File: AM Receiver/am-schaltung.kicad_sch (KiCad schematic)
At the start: 43 parts, among them IC100 SA612AD, IC103 TDA1072AT, P100 10k 25% Trimmer, Q100 MMBFJ310LT3G, Q101 MMBFJ310LT3G

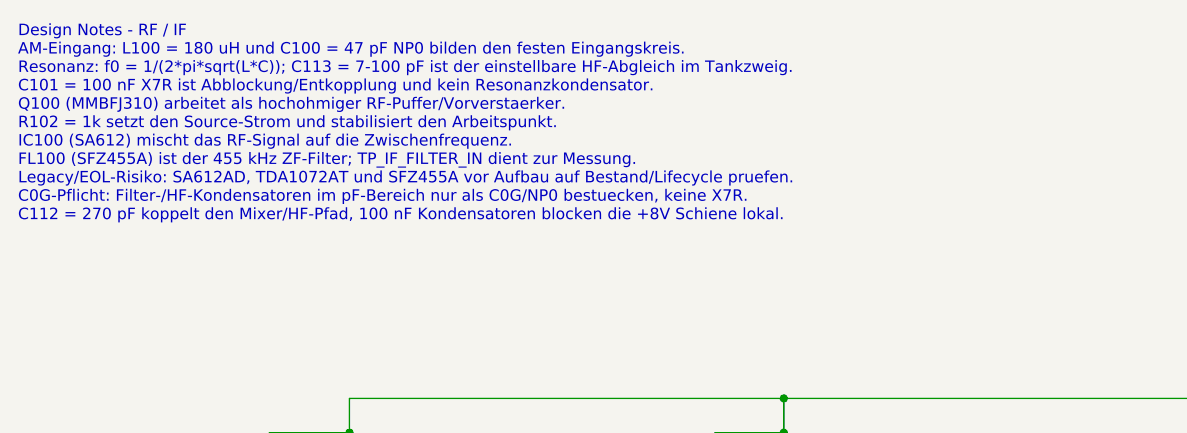
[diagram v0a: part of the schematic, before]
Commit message: updated schematic root page voltage
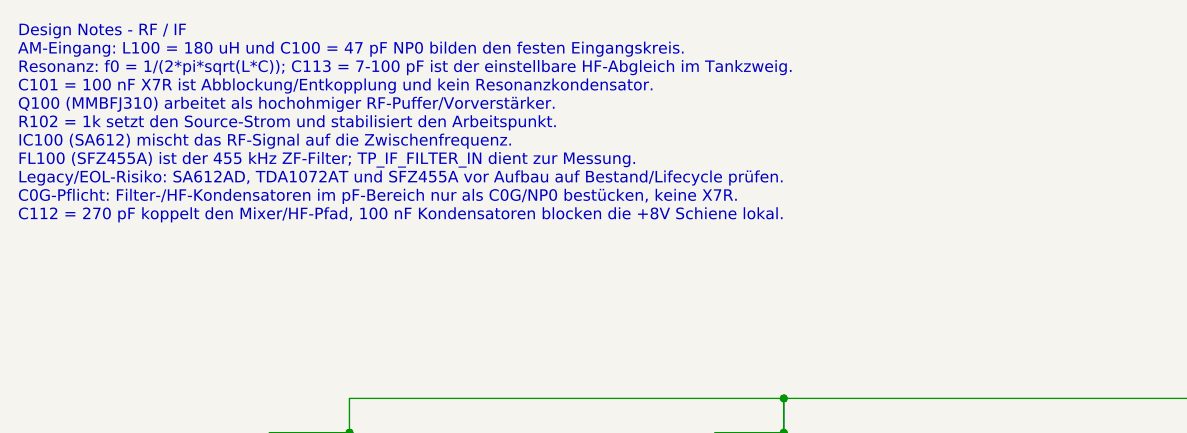
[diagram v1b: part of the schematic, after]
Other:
- note added: "Design Notes - RF / IF AM-Eingang: L100 = 180 uH und C100 = 47 pF NP0 bilden den festen Eingangskreis. Resonanz: f0 = 1/(2*pi*sqrt(L*C)); C113 = 7-100 pF ist der einstellbare HF-Abgleich im Tankzweig. C101 = 100 nF X7R ist Abblockung/Entkopplung und kein Resonanzkondensator. Q100 (MMBFJ310) arbeitet als hochohmiger RF-Puffer/Vorverstärker. R102 = 1k setzt den Source-Strom und stabilisiert den Arb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"
- note removed: "Design Notes - RF / IF AM-Eingang: L100 = 180 uH und C100 = 47 pF NP0 bilden den festen Eingangskreis. Resonanz: f0 = 1/(2*pi*sqrt(L*C)); C113 = 7-100 pF ist der einstellbare HF-Abgleich im Tankzweig. C101 = 100 nF X7R ist Abblockung/Entkopplung und kein Resonanzkondensator. Q100 (MMBFJ310) arbeitet als hochohmiger RF-Puffer/Vorverstaerker. R102 = 1k setzt den Source-Strom und stabilisiert den Ar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"
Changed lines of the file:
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@@
 		(comment 3 "T. Brown")
 	)
-	(text "Design Notes - RF / IF\nAM-Eingang: L100 = 180 uH und C100 = 47 pF NP0 bilden den festen Eingangskreis.\nResonanz: f0 = 1/(2*pi*sqrt(L*C)); C113 = 7-100 pF ist der einstellbare HF-Abgleich im Tankzweig.\nC101 = 100 nF X7R ist Abblockung/Entkopplung und kein Resonanzkondensator.\nQ100 (MMBFJ310) arbeitet als hochohmiger RF-Puffer/Vorverstaerker.\nR102 = 1k setzt den Source-Strom und stabilisiert den Arbeitspunkt.\nIC100 (SA612) mischt das RF-Signal auf die Zwischenfrequenz.\nFL100 (SFZ455A) ist der 455 kHz ZF-Filter; TP_IF_FILTER_IN dient zur Messung.\nLegacy/EOL-Risiko: SA612AD, TDA1072AT und SFZ455A vor Aufbau auf Bestand/Lifecycle pruefen.\nC0G-Pflicht: Filter-/HF-Kondensatoren im pF-Bereich nur als C0G/NP0 bestuecken, keine X7R.\nC112 = 270 pF koppelt den Mixer/HF-Pfad, 100 nF Kondensatoren blocken die +8V Schiene lokal."
+	(text "Design Notes - RF / IF\nAM-Eingang: L100 = 180 uH und C100 = 47 pF NP0 bilden den festen Eingangskreis.\nResonanz: f0 = 1/(2*pi*sqrt(L*C)); C113 = 7-100 pF ist der einstellbare HF-Abgleich im Tankzweig.\nC101 = 100 nF X7R ist Abblockung/Entkopplung und kein Resonanzkondensator.\nQ100 (MMBFJ310) arbeitet als hochohmiger RF-Puffer/Vorverstärker.\nR102 = 1k setzt den Source-Strom und stabilisiert den Arbeitspunkt.\nIC100 (SA612) mischt das RF-Signal auf die Zwischenfrequenz.\nFL100 (SFZ455A) ist der 455 kHz ZF-Filter; TP_IF_FILTER_IN dient zur Messung.\nLegacy/EOL-Risiko: SA612AD, TDA1072AT und SFZ455A vor Aufbau auf Bestand/Lifecycle prüfen.\nC0G-Pflicht: Filter-/HF-Kondensatoren im pF-Bereich nur als C0G/NP0 bestücken, keine X7R.\nC112 = 270 pF koppelt den Mixer/HF-Pfad, 100 nF Kondensatoren blocken die +8V Schiene lokal."
 		(exclude_from_sim no)
 		(at 35.56 34.29 0)

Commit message: Updated Deckblatt
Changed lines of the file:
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@@
 		)
 		(property "Value" "100n/50V X7R 10%"
-			(at 131.445 119.38 0)
+			(at 131.318 120.396 0)
 			(show_name no)
 			(do_not_autoplace no)
@@
 		)
 		(property "Value" "7-100p/200V"
-			(at 148.59 119.126 0)
-			(show_name no)
-			(do_not_autoplace no)
+			(at 156.972 118.872 0)
+			(show_name no)
+			(do_not_autoplace no)
